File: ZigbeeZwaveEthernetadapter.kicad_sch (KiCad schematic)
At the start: 16 parts, among them J1 Barrel_Jack, J11 Conn_02x06_Odd_Even, J12 Conn_01x06, J14 Conn_01x06, J2 USB_B_Micro, J21 Conn_02x06_Odd_Even, J22 Conn_01x06, J24 Conn_01x06, J3 USB4125-GF-A, J31 Conn_02x05_Odd_Even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

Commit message: Mod: Assigned the footprints of the pin header and sockets
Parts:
- J1: footprint Connector_BarrelJack:BarrelJack_SwitchcraftConxall_RAPC10U_Horizontal -> (none)
- J11: footprint Connector_PinHeader_2.54mm:PinHeader_2x06_P2.54mm_Vertical -> Connector_PinSocket_2.54mm:PinSocket_2x06_P2.54mm_Vertical
- J12, J14: footprint (none) -> Connector_PinSocket_2.54mm:PinSocket_1x06_P2.54mm_Vertical
- J22, J24: footprint (none) -> Connector_PinHeader_2.54mm:PinHeader_1x06_P2.54mm_Vertical
- J31: footprint (none) -> Connector_PinHeader_2.54mm:PinHeader_2x05_P2.54mm_Vertical
- J41: footprint (none) -> Connector_PinHeader_2.54mm:PinHeader_1x05_P2.54mm_Vertical
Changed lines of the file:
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@@
     (property "Reference" "J14" (id 0) (at 50.8 133.35 0))
     (property "Value" "Conn_01x06" (id 1) (at 50.8 135.89 0))
-    (property "Footprint" "" (id 2) (at 50.8 144.78 0)
+    (property "Footprint" "Connector_PinSocket_2.54mm:PinSocket_1x06_P2.54mm_Vertical" (id 2) (at 50.8 144.78 0)
       (effects (font (size 1.27 1.27)) hide)
     )
@@
     (property "Reference" "J31" (id 0) (at 165.1 31.75 0))
     (property "Value" "Conn_02x05_Odd_Even" (id 1) (at 165.1 34.29 0))
-    (property "Footprint" "" (id 2) (at 163.83 43.18 0)
+    (property "Footprint" "Connector_PinHeader_2.54mm:PinHeader_2x05_P2.54mm_Vertical" (id 2) (at 163.83 43.18 0)
       (effects (font (size 1.27 1.27)) hide)
     )
@@
     (property "Reference" "J11" (id 0) (at 50.8 31.75 0))
     (property "Value" "Conn_02x06_Odd_Even" (id 1) (at 50.8 34.29 0))
-    (property "Footprint" "Connector_PinHeader_2.54mm:PinHeader_2x06_P2.54mm_Vertical" (id 2) (at 49.53 43.18 0)
+    (property "Footprint" "Connector_PinSocket_2.54mm:PinSocket_2x06_P2.54mm_Vertical" (id 2) (at 49.53 43.18 0)
       (effects (font (size 1.27 1.27)) hide)
     )
@@
       (effects (font (size 1.27 1.27)) (justify right))
     )
-    (property "Footprint" "Connector_BarrelJack:BarrelJack_SwitchcraftConxall_RAPC10U_Horizontal" (id 2) (at 234.95 143.256 0)
+    (property "Footprint" "" (id 2) (at 234.95 143.256 0)
       (effects (font (size 1.27 1.27)) hide)
     )
@@
     (property "Reference" "J12" (id 0) (at 50.8 82.55 0))
     (property "Value" "Conn_01x06" (id 1) (at 50.8 85.09 0))
-    (property "Footprint" "" (id 2) (at 50.8 93.98 0)
+    (property "Footprint" "Connector_PinSocket_2.54mm:PinSocket_1x06_P2.54mm_Vertical" (id 2) (at 50.8 93.98 0)
       (effects (font (size 1.27 1.27)) hide)
     )
@@
       (effects (font (size 1.27 1.27)) (justify left))
     )
-    (property "Footprint" "" (id 2) (at 76.2 93.98 0)
+    (property "Footprint" "Connector_PinHeader_2.54mm:PinHeader_1x06_P2.54mm_Vertical" (id 2) (at 76.2 93.98 0)
       (effects (font (size 1.27 1.27)) hide)
     )
@@
     (property "Reference" "J41" (id 0) (at 127 31.75 0))
     (property "Value" "Conn_01x05" (id 1) (at 127 34.29 0))
-    (property "Footprint" "" (id 2) (at 127 43.18 0)
+    (property "Footprint" "Connector_PinHeader_2.54mm:PinHeader_1x05_P2.54mm_Vertical" (id 2) (at 127 43.18 0)
       (effects (font (size 1.27 1.27)) hide)
     )
@@
       (effects (font (size 1.27 1.27)) (justify left))
     )
-    (property "Footprint" "" (id 2) (at 76.2 144.78 0)
+    (property "Footprint" "Connector_PinHeader_2.54mm:PinHeader_1x06_P2.54mm_Vertical" (id 2) (at 76.2 144.78 0)
       (effects (font (size 1.27 1.27)) hide)
     )
@@
     )
     (path "/45ccafcf-91a6-475a-88ef-bc1903af912b"
-      (reference "J1") (unit 1) (value "Barrel_Jack") (footprint "Connector_BarrelJack:BarrelJack_SwitchcraftConxall_RAPC10U_Horizontal")
+      (reference "J1") (unit 1) (value "Barrel_Jack") (footprint "")
     )
     (path "/0f5191d7-13d2-4136-8d2a-cb1379a2e5b4"
@@
     )
     (path "/3b55a99d-348c-40f8-9a69-dea028a2f9d2"
-      (reference "J11") (unit 1) (value "Conn_02x06_Odd_Even") (footprint "Connector_PinHeader_2.54mm:PinHeader_2x06_P2.54mm_Vertical")
+      (reference "J11") (unit 1) (value "Conn_02x06_Odd_Even") (footprint "Connector_PinSocket_2.54mm:PinSocket_2x06_P2.54mm_Vertical")
     )
     (path "/540f9e89-dc5a-45d1-a00c-5d874aea0f75"
-      (reference "J12") (unit 1) (value "Conn_01x06") (footprint "")
+      (reference "J12") (unit 1) (value "Conn_01x06") (footprint "Connector_PinSocket_2.54mm:PinSocket_1x06_P2.54mm_Vertical")
     )
     (path "/2505202c-591d-4186-8e12-ee0c3119edf4"
-      (reference "J14") (unit 1) (value "Conn_01x06") (footprint "")
+      (reference "J14") (unit 1) (value "Conn_01x06") (footprint "Connector_PinSocket_2.54mm:PinSocket_1x06_P2.54mm_Vertical")
     )
     (path "/bbe0fc49-d4b1-4d81-8535-859e0ea4372a"
@@
     )
     (path "/5dd7f8fc-1f78-4714-9c47-ca33ef162f17"
-      (reference "J22") (unit 1) (value "Conn_01x06") (footprint "")
+      (reference "J22") (unit 1) (value "Conn_01x06") (footprint "Connector_PinHeader_2.54mm:PinHeader_1x06_P2.54mm_Vertical")
     )
     (path "/cb972e35-ad0c-4d8f-952c-98c3326d888f"
-      (reference "J24") (unit 1) (value "Conn_01x06") (footprint "")
+      (reference "J24") (unit 1) (value "Conn_01x06") (footprint "Connector_PinHeader_2.54mm:PinHeader_1x06_P2.54mm_Vertical")
     )
     (path "/3255fb95-52a3-4ca4-ad63-bdc6a222c289"
-      (reference "J31") (unit 1) (value "Conn_02x05_Odd_Even") (footprint "")
+      (reference "J31") (unit 1) (value "Conn_02x05_Odd_Even") (footprint "Connector_PinHeader_2.54mm:PinHeader_2x05_P2.54mm_Vertical")
     )
     (path "/77b4b51b-01df-47b3-b8dc-d4db02b7ea93"
-      (reference "J41") (unit 1) (value "Conn_01x05") (footprint "")
+      (reference "J41") (unit 1) (value "Conn_01x05") (footprint "Connector_PinHeader_2.54mm:PinHeader_1x05_P2.54mm_Vertical")
     )
     (path "/d49ff4f7-f21e-48b4-ba82-133b511a6548"

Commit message: Mod: Assigned more footprints to the capacitors and resistors
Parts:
- C1: value 0.47µ -> 47µ; footprint (none) -> Capacitor_SMD:C_0805_2012Metric_Pad1.18x1.45mm_HandSolder
- C2: value 33µ -> 0.47µ; footprint (none) -> Capacitor_SMD:C_0805_2012Metric_Pad1.18x1.45mm_HandSolder
- R1, R2: footprint (none) -> Resistor_SMD:R_0805_2012Metric_Pad1.20x1.40mm_HandSolder
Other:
- note added: "Note: Symbol and Package must be changed."
- note removed: "Note: Symbol and Package must be changed. and Capacitor values gets updated on what we have in stock. C1 is the min. value of the Cap to be stable so choose a bigger one"
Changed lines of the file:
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@@
     (effects (font (size 1.27 1.27)) (justify left bottom))
   )
-  (text "Note: Symbol and Package must be changed.\nand Capacitor values gets updated on what\nwe have in stock. C1 is the min. value of the\nCap to be stable so choose a bigger one"
-    (at 154.94 133.35 0)
+  (text "Note: Symbol and Package must be changed." (at 156.21 127 0)
     (effects (font (size 1.27 1.27)) (justify left bottom))
   )
@@
     )
     (pin "1")
-  )
-  (symbol (lib_id "Device:C") (at 193.04 107.95 0) (unit 1)
-    (in_bom yes) (on_board yes) (fields_autoplaced)
-    (property "Reference" "C2" (id 0) (at 196.85 106.6799 0)
-      (effects (font (size 1.27 1.27)) (justify left))
-    )
-    (property "Value" "33µ" (id 1) (at 196.85 109.2199 0)
-      (effects (font (size 1.27 1.27)) (justify left))
-    )
-    (property "Footprint" "" (id 2) (at 194.0052 111.76 0)
-      (effects (font (size 1.27 1.27)) hide)
-    )
-    (property "Datasheet" "~" (id 3) (at 193.04 107.95 0)
-      (effects (font (size 1.27 1.27)) hide)
-    )
-    (pin "1")
-    (pin "2")
   )
   (symbol (lib_id "Connector:USB_B_Micro") (at 236.22 106.68 0) (mirror y) (unit 1)
@@
     )
     (pin "1")
+  )
+  (symbol (lib_id "Device:C") (at 162.56 107.95 0) (unit 1)
+    (in_bom yes) (on_board yes) (fields_autoplaced)
+    (property "Reference" "C1" (id 0) (at 166.37 106.6799 0)
+      (effects (font (size 1.27 1.27)) (justify left))
+    )
+    (property "Value" "47µ" (id 1) (at 166.37 109.2199 0)
+      (effects (font (size 1.27 1.27)) (justify left))
+    )
+    (property "Footprint" "Capacitor_SMD:C_0805_2012Metric_Pad1.18x1.45mm_HandSolder" (id 2) (at 163.5252 111.76 0)
+      (effects (font (size 1.27 1.27)) hide)
+    )
+    (property "Datasheet" "https://www.digikey.ch/de/products/detail/murata-electronics/GRM21BR61A476ME15L/4905529" (id 3) (at 162.56 107.95 0)
+      (effects (font (size 1.27 1.27)) hide)
+    )
+    (pin "1")
+    (pin "2")
   )
   (symbol (lib_id "power:+5V") (at 223.52 35.56 0) (unit 1)
@@
     (pin "3")
   )
+  (symbol (lib_id "Device:C") (at 193.04 107.95 0) (unit 1)
+    (in_bom yes) (on_board yes) (fields_autoplaced)
+    (property "Reference" "C2" (id 0) (at 196.85 106.6799 0)
+      (effects (font (size 1.27 1.27)) (justify left))
+    )
+    (property "Value" "0.47µ" (id 1) (at 196.85 109.2199 0)
+      (effects (font (size 1.27 1.27)) (justify left))
+    )
+    (property "Footprint" "Capacitor_SMD:C_0805_2012Metric_Pad1.18x1.45mm_HandSolder" (id 2) (at 194.0052 111.76 0)
+      (effects (font (size 1.27 1.27)) hide)
+    )
+    (property "Datasheet" "https://www.digikey.ch/de/products/detail/murata-electronics/GRM21BR71H474KA88L/702592" (id 3) (at 193.04 107.95 0)
+      (effects (font (size 1.27 1.27)) hide)
+    )
+    (pin "1")
+    (pin "2")
+  )
   (symbol (lib_id "power:+3V3") (at 36.83 35.56 0) (unit 1)
     (in_bom yes) (on_board yes) (fields_autoplaced)
@@
     (pin "6")
   )
-  (symbol (lib_id "Device:C") (at 162.56 107.95 0) (unit 1)
-    (in_bom yes) (on_board yes) (fields_autoplaced)
-    (property "Reference" "C1" (id 0) (at 166.37 106.6799 0)
-      (effects (font (size 1.27 1.27)) (justify left))
-    )
-    (property "Value" "0.47µ" (id 1) (at 166.37 109.2199 0)
-      (effects (font (size 1.27 1.27)) (justify left))
-    )
-    (property "Footprint" "" (id 2) (at 163.5252 111.76 0)
-      (effects (font (size 1.27 1.27)) hide)
-    )
-    (property "Datasheet" "~" (id 3) (at 162.56 107.95 0)
-      (effects (font (size 1.27 1.27)) hide)
-    )
-    (pin "1")
-    (pin "2")
-  )
   (symbol (lib_id "Device:R") (at 208.28 54.61 0) (unit 1)
     (in_bom yes) (on_board yes) (fields_autoplaced)
@@
       (effects (font (size 1.27 1.27)) (justify left))
     )
-    (property "Footprint" "" (id 2) (at 206.502 54.61 90)
+    (property "Footprint" "Resistor_SMD:R_0805_2012Metric_Pad1.20x1.40mm_HandSolder" (id 2) (at 206.502 54.61 90)
       (effects (font (size 1.27 1.27)) hide)
     )
@@
       (effects (font (size 1.27 1.27)) (justify left))
     )
-    (property "Footprint" "" (id 2) (at 219.202 54.61 90)
+    (property "Footprint" "Resistor_SMD:R_0805_2012Metric_Pad1.20x1.40mm_HandSolder" (id 2) (at 219.202 54.61 90)
       (effects (font (size 1.27 1.27)) hide)
     )
@@
       (reference "#PWR024") (unit 1) (value "GND") (footprint "")
     )
-    (path "/ce9a570a-5e1a-4650-bd4b-81e7c520e33e"
-      (reference "C1") (unit 1) (value "0.47µ") (footprint "")
-    )
-    (path "/0b2d7c04-7285-40e3-810d-442abf84c149"
-      (reference "C2") (unit 1) (value "33µ") (footprint "")
+    (path "/2198040d-d00b-4b4c-8ebb-f2c24addce0e"
+      (reference "C1") (unit 1) (value "47µ") (footprint "Capacitor_SMD:C_0805_2012Metric_Pad1.18x1.45mm_HandSolder")
+    )
+    (path "/27932f6d-7eee-4ca5-abf5-70d14d5611df"
+      (reference "C2") (unit 1) (value "0.47µ") (footprint "Capacitor_SMD:C_0805_2012Metric_Pad1.18x1.45mm_HandSolder")
     )
     (path "/45ccafcf-91a6-475a-88ef-bc1903af912b"
@@
     )
     (path "/d49ff4f7-f21e-48b4-ba82-133b511a6548"
-      (reference "R1") (unit 1) (value "5.1k") (footprint "")
+      (reference "R1") (unit 1) (value "5.1k") (footprint "Resistor_SMD:R_0805_2012Metric_Pad1.20x1.40mm_HandSolder")
     )
     (path "/d829965d-02b1-4e7e-9b65-986c63780732"
-      (reference "R2") (unit 1) (value "5.1k") (footprint "")
+      (reference "R2") (unit 1) (value "5.1k") (footprint "Resistor_SMD:R_0805_2012Metric_Pad1.20x1.40mm_HandSolder")
     )
     (path "/275839e4-00de-4be8-83f2-680a421afcba"

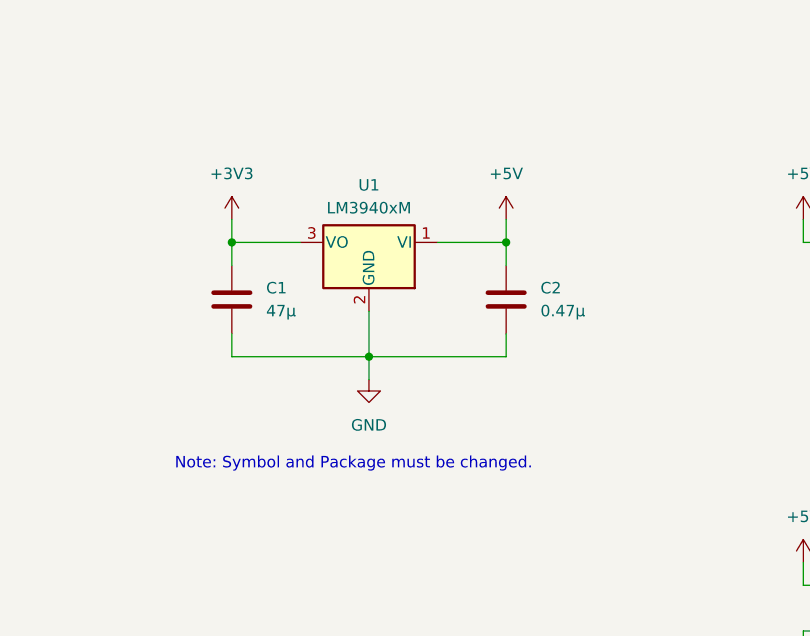
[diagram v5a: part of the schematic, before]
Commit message: Mod: Assigned footprint for LDO, Micro USB and Barrel-Jack
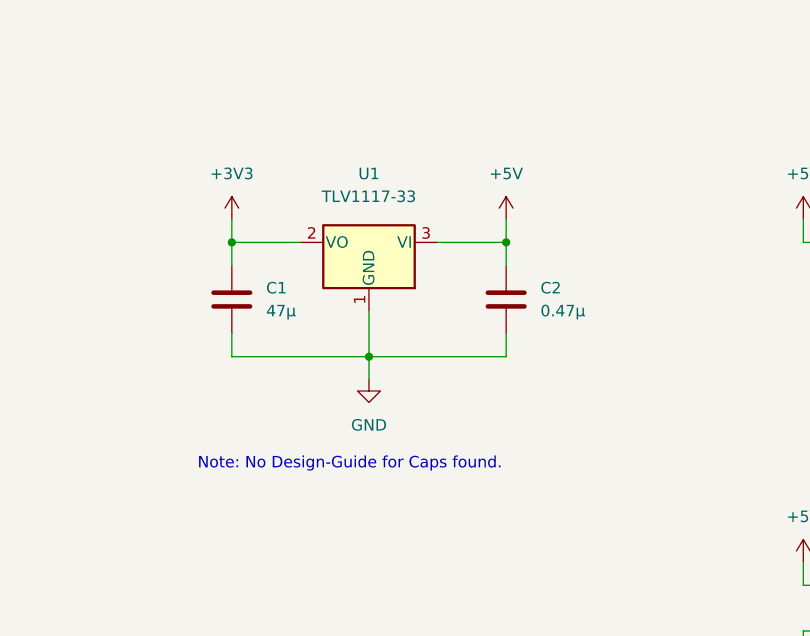
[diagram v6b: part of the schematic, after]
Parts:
- removed U1: LM3940xM, symbol Regulator_Linear:LM2937xS
- added U1: TLV1117-33, symbol Regulator_Linear:TLV1117-33
- J1: footprint (none) -> connectors:PJ-037A
- J2: footprint (none) -> connectors:AMPHENOL_10118194-0001LF
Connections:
- net +3V3: now also U1.2 (VO)
- net +5V: now also U1.3 (VI)
- net GND: now also U1.1 (GND)
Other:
- note added: "Note: No Design-Guide for Caps found."
- note removed: "Note: Symbol and Package must be changed."
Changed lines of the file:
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@@
     (effects (font (size 1.27 1.27)) (justify left bottom))
   )
-  (text "Note: Symbol and Package must be changed." (at 156.21 127 0)
+  (text "Note: No Design-Guide for Caps found." (at 158.75 127 0)
     (effects (font (size 1.27 1.27)) (justify left bottom))
   )
@@
       (effects (font (size 1.27 1.27)) (justify right))
     )
-    (property "Footprint" "" (id 2) (at 232.41 107.95 0)
+    (property "Footprint" "connectors:AMPHENOL_10118194-0001LF" (id 2) (at 232.41 107.95 0)
       (effects (font (size 1.27 1.27)) hide)
     )
@@
     (pin "5")
     (pin "6")
-  )
-  (symbol (lib_id "Regulator_Linear:LM2937xS") (at 177.8 101.6 0) (mirror y) (unit 1)
-    (in_bom yes) (on_board yes)
-    (property "Reference" "U1" (id 0) (at 177.8 95.25 0))
-    (property "Value" "LM3940xM" (id 1) (at 177.8 97.79 0))
-    (property "Footprint" "" (id 2) (at 177.8 95.885 0)
-      (effects (font (size 1.27 1.27) italic) hide)
-    )
-    (property "Datasheet" "" (id 3) (at 177.8 102.87 0)
-      (effects (font (size 1.27 1.27)) hide)
-    )
-    (pin "1")
-    (pin "2")
-    (pin "3")
   )
   (symbol (lib_id "Device:C") (at 193.04 107.95 0) (unit 1)
@@
       (effects (font (size 1.27 1.27)) (justify right))
     )
-    (property "Footprint" "" (id 2) (at 234.95 143.256 0)
+    (property "Footprint" "connectors:PJ-037A" (id 2) (at 234.95 143.256 0)
       (effects (font (size 1.27 1.27)) hide)
     )
@@
     (pin "5")
     (pin "6")
+  )
+  (symbol (lib_id "Regulator_Linear:TLV1117-33") (at 177.8 101.6 0) (mirror y) (unit 1)
+    (in_bom yes) (on_board yes) (fields_autoplaced)
+    (property "Reference" "U1" (id 0) (at 177.8 93.98 0))
+    (property "Value" "TLV1117-33" (id 1) (at 177.8 96.52 0))
+    (property "Footprint" "" (id 2) (at 177.8 101.6 0)
+      (effects (font (size 1.27 1.27)) hide)
+    )
+    (property "Datasheet" "http://www.ti.com/lit/ds/symlink/tlv1117.pdf" (id 3) (at 177.8 101.6 0)
+      (effects (font (size 1.27 1.27)) hide)
+    )
+    (pin "1")
+    (pin "2")
+    (pin "3")
   )
   (symbol (lib_id "Device:R") (at 208.28 54.61 0) (unit 1)
@@
     )
     (path "/45ccafcf-91a6-475a-88ef-bc1903af912b"
-      (reference "J1") (unit 1) (value "Barrel_Jack") (footprint "")
+      (reference "J1") (unit 1) (value "Barrel_Jack") (footprint "connectors:PJ-037A")
     )
     (path "/0f5191d7-13d2-4136-8d2a-cb1379a2e5b4"
-      (reference "J2") (unit 1) (value "USB_B_Micro") (footprint "")
+      (reference "J2") (unit 1) (value "USB_B_Micro") (footprint "connectors:AMPHENOL_10118194-0001LF")
     )
     (path "/f71369f0-fe7d-4e5f-876d-a5b0df357ba9"
@@
       (reference "R2") (unit 1) (value "5.1k") (footprint "Resistor_SMD:R_0805_2012Metric_Pad1.20x1.40mm_HandSolder")
     )
-    (path "/275839e4-00de-4be8-83f2-680a421afcba"
-      (reference "U1") (unit 1) (value "LM3940xM") (footprint "")
-    )
-  )
+    (path "/ce0c3e64-c9ac-47d9-8ade-14119a95fc68"
+      (reference "U1") (unit 1) (value "TLV1117-33") (footprint "Package_TO_SOT_SMD:SOT-223-3_TabPin2")
+    )
+  )

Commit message: Mod: Changed footprint of U1
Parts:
- U1: footprint (none) -> Package_TO_SOT_SMD:SOT-223-3_TabPin2
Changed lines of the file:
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@@
     (property "Reference" "U1" (id 0) (at 177.8 93.98 0))
     (property "Value" "TLV1117-33" (id 1) (at 177.8 96.52 0))
-    (property "Footprint" "" (id 2) (at 177.8 101.6 0)
+    (property "Footprint" "Package_TO_SOT_SMD:SOT-223-3_TabPin2" (id 2) (at 177.8 101.6 0)
       (effects (font (size 1.27 1.27)) hide)
     )
